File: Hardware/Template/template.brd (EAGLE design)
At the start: 39.4 x 39.4 mm, 24 parts, among them J1 10144517-042802LF, J2 10144518-041802LF, J3 10144517-042802LF, J4 10144518-041802LF, J6 2X5_0.05_SWD, U6 NCV8170AXV330T2G, U7 ATA6561-GAQW-N

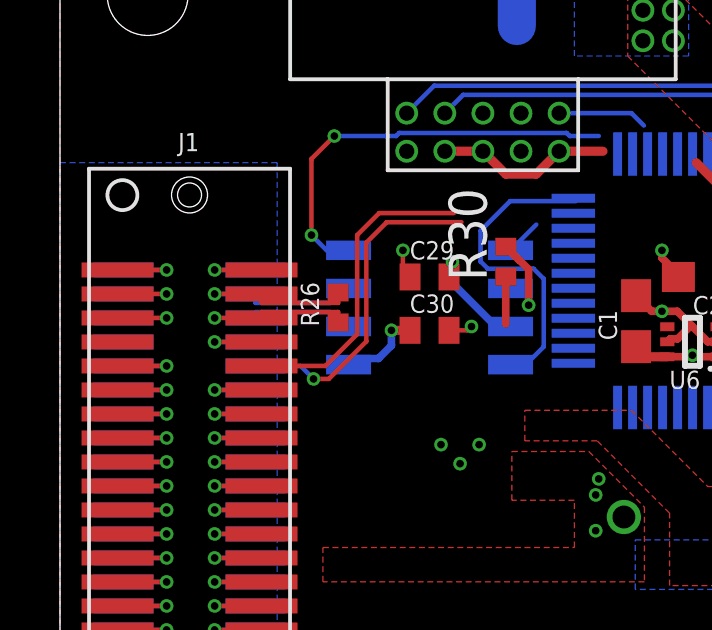
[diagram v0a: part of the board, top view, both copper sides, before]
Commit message: fixed power rail naming in template and added inventor drawing
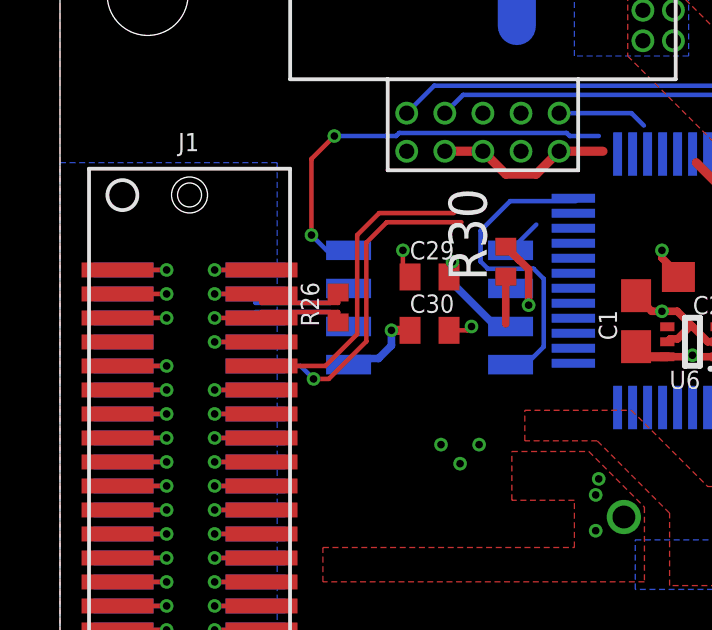
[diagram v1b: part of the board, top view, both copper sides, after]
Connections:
- new net +12V: J3.17, J3.19, J3.21, J3.23, J3.25, J3.27, J3.29, J4.17, J4.19, J4.21, J4.23, J4.25, J4.27, J4.29
- net +5V: no longer J3.17, J3.19, J3.21, J3.23, J3.25, J3.27, J3.29, J4.17, J4.19, J4.21, J4.23, J4.25, J4.27, J4.29
- net CAN0_N: now also J1.6
- net CAN_N: no longer J1.6
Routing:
- net +5V: track 10.9 -> 6.71 mm
- net +12V: track 0.00 -> 4.22 mm
- net CAN_N: track 7.96 -> 6.20 mm, vias 1 -> 0
- net CAN0_N: track 0.00 -> 1.56 mm, vias 0 -> 1
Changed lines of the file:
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@@
 <?xml version="1.0" encoding="utf-8"?>
 <!DOCTYPE eagle SYSTEM "eagle.dtd">
-<eagle version="9.5.2">
+<eagle version="9.6.0">
 <drawing>
 <settings>
-<setting alwaysvectorfont="no"/>
+<setting alwaysvectorfont="yes"/>
 <setting verticaltext="up"/>
 </settings>
@@
 </layers>
 <board>
-<fusionsync huburn="a.cGVyc29uYWw6dWUyZDEyOGNj" projecturn="a.cGVyc29uYWw6dWUyZDEyOGNjIzIwMTkwOTMwMjIwNjQ4MDc2" f3durn="urn:adsk.wipprod:dm.lineage:ArUQAsjyQquSRS0aqH2C6A" pcbguid="3c4015e3-43ac-4e19-9fe8-228eb0397e7d" lastpulledtime="" lastsyncedchangeguid="2c83db97-9ebd-c503-bffe-3982d56f7fbb"/>
+<fusionsync huburn="a.cGVyc29uYWw6dWUyZDEyOGNj" projecturn="a.cGVyc29uYWw6dWUyZDEyOGNjIzIwMTkwOTMwMjIwNjQ4MDc2" f3durn="urn:adsk.wipprod:dm.lineage:ArUQAsjyQquSRS0aqH2C6A" pcbguid="3c4015e3-43ac-4e19-9fe8-228eb0397e7d" lastpulledtime="" lastsyncedchangeguid="2c83db97-9ebd-c503-bffe-3982d56f7fbb" latestrevisionid="" lastsyncedrevisionid="" lastboardhashguid="" lastpushedtime="" linktopcb3d="%12"/>
 <plain>
 <wire x1="0" y1="36.449" x2="0" y2="2.921" width="0" layer="20"/>
@@
 <signal name="CAN_N">
 <contactref element="U7" pad="6"/>
-<contactref element="J1" pad="6"/>
-<wire x1="6.718" y1="25.685" x2="6.718" y2="25.8826" width="0.1524" layer="1"/>
 <wire x1="6.718" y1="25.8826" x2="9.271" y2="25.8826" width="0.1524" layer="1"/>
 <wire x1="9.271" y1="25.8826" x2="9.271" y2="25.535" width="0.1524" layer="1"/>
@@
 <wire x1="9.4996" y1="25.4" x2="9.017" y2="25.8826" width="0.1524" layer="16"/>
 <contactref element="R26" pad="1"/>
-<via x="5.154" y="25.685" extent="1-16" drill="0.254"/>
-<wire x1="5.154" y1="25.685" x2="6.718" y2="25.685" width="0.1524" layer="1"/>
-<wire x1="6.718" y1="25.685" x2="6.518" y2="25.8826" width="0" layer="19" extent="1-16"/>
+<wire x1="6.518" y1="25.8826" x2="6.718" y2="25.8826" width="0" layer="19" extent="1-16"/>
 </signal>
 <signal name="DETECT_A">
@@
 <wire x1="13.081" y1="26.8445" x2="13.081" y2="27.559" width="0.254" layer="16"/>
 <wire x1="14.5255" y1="25.4" x2="13.081" y2="26.8445" width="0.254" layer="16"/>
-<contactref element="J3" pad="29"/>
-<contactref element="J3" pad="17"/>
-<contactref element="J3" pad="19"/>
-<contactref element="J3" pad="21"/>
-<contactref element="J3" pad="23"/>
-<contactref element="J3" pad="25"/>
-<contactref element="J3" pad="27"/>
-<contactref element="J4" pad="17"/>
-<contactref element="J4" pad="19"/>
-<contactref element="J4" pad="21"/>
-<contactref element="J4" pad="23"/>
-<contactref element="J4" pad="25"/>
-<contactref element="J4" pad="27"/>
-<contactref element="J4" pad="29"/>
-<wire x1="33.106" y1="16.085" x2="33.4274" y2="16.4064" width="0.1524" layer="16"/>
 <via x="30.861" y="20.701" extent="1-16" drill="0.254"/>
 <polygon width="0.1524" layer="16" thermals="no">
@@
 <via x="31.115" y="20.193" extent="1-16" drill="0.254"/>
 <via x="31.369" y="19.685" extent="1-16" drill="0.254"/>
-<wire x1="30.601" y1="16.885" x2="33.106" y2="16.885" width="0.1524" layer="16"/>
-<wire x1="29.71" y1="15.994" x2="30.601" y2="16.885" width="0.1524" layer="16"/>
-<wire x1="32.906" y1="20.885" x2="33.106" y2="20.885" width="0" layer="19" extent="1-16"/>
-<wire x1="33.106" y1="20.085" x2="33.106" y2="20.885" width="0" layer="19" extent="16-16"/>
-<wire x1="32.906" y1="20.085" x2="33.106" y2="20.085" width="0" layer="19" extent="1-16"/>
-<wire x1="33.106" y1="19.285" x2="33.106" y2="20.085" width="0" layer="19" extent="16-16"/>
-<wire x1="32.906" y1="19.285" x2="33.106" y2="19.285" width="0" layer="19" extent="1-16"/>
-<wire x1="33.106" y1="18.485" x2="33.106" y2="19.285" width="0" layer="19" extent="16-16"/>
-<wire x1="32.906" y1="18.485" x2="33.106" y2="18.485" width="0" layer="19" extent="1-16"/>
-<wire x1="33.106" y1="17.685" x2="33.106" y2="18.485" width="0" layer="19" extent="16-16"/>
-<wire x1="32.906" y1="17.685" x2="33.106" y2="17.685" width="0" layer="19" extent="1-16"/>
-<wire x1="32.906" y1="16.885" x2="32.906" y2="17.685" width="0" layer="19" extent="1-1"/>
-<wire x1="33.106" y1="16.885" x2="32.906" y2="16.885" width="0" layer="19" extent="1-16"/>
-<wire x1="33.4274" y1="16.4064" x2="33.106" y2="16.885" width="0" layer="19" extent="16-16"/>
-<wire x1="32.906" y1="16.085" x2="33.106" y2="16.085" width="0" layer="19" extent="1-16"/>
-<wire x1="33.106" y1="15.285" x2="33.106" y2="16.085" width="0" layer="19" extent="16-16"/>
-<wire x1="32.906" y1="15.285" x2="33.106" y2="15.285" width="0" layer="19" extent="1-16"/>
+<wire x1="31.369" y1="20.701" x2="30.861" y2="20.701" width="0" layer="19" extent="1-1"/>
+<wire x1="31.115" y1="20.193" x2="30.861" y2="20.701" width="0" layer="19" extent="1-1"/>
+<wire x1="31.369" y1="19.685" x2="31.115" y2="20.193" width="0" layer="19" extent="1-1"/>
+<wire x1="32.906" y1="15.285" x2="31.369" y2="19.685" width="0" layer="19" extent="1-1"/>
+<wire x1="33.106" y1="15.285" x2="32.906" y2="15.285" width="0" layer="19" extent="1-16"/>
 <wire x1="33.106" y1="14.485" x2="33.106" y2="15.285" width="0" layer="19" extent="16-16"/>
 <wire x1="32.906" y1="14.485" x2="33.106" y2="14.485" width="0" layer="19" extent="1-16"/>
@@
 <wire x1="33.106" y1="12.885" x2="33.106" y2="13.685" width="0" layer="19" extent="16-16"/>
 <wire x1="32.906" y1="12.885" x2="33.106" y2="12.885" width="0" layer="19" extent="1-16"/>
-<wire x1="31.369" y1="20.701" x2="32.906" y2="20.885" width="0" layer="19" extent="1-1"/>
-<wire x1="30.861" y1="20.701" x2="31.369" y2="20.701" width="0" layer="19" extent="1-1"/>
-<wire x1="31.115" y1="20.193" x2="31.369" y2="20.701" width="0" layer="19" extent="1-1"/>
-<wire x1="31.369" y1="19.685" x2="31.115" y2="20.193" width="0" layer="19" extent="1-1"/>
 <wire x1="31.242" y1="14.732" x2="32.906" y2="14.485" width="0" layer="19" extent="1-1"/>
 <wire x1="31.242" y1="13.97" x2="31.242" y2="14.732" width="0" layer="19" extent="1-1"/>
@@
 <signal name="CAN0_N">
 <contactref element="J2" pad="6"/>
+<contactref element="J1" pad="6"/>
+<via x="5.154" y="25.685" extent="1-16" drill="0.254"/>
+<wire x1="5.154" y1="25.685" x2="6.718" y2="25.685" width="0.1524" layer="1"/>
+<wire x1="6.718" y1="25.685" x2="6.518" y2="25.685" width="0" layer="19" extent="1-16"/>
+</signal>
+<signal name="+12V">
+<contactref element="J3" pad="29"/>
+<contactref element="J3" pad="17"/>
+<contactref element="J3" pad="19"/>
+<contactref element="J3" pad="21"/>
+<contactref element="J3" pad="23"/>
+<contactref element="J3" pad="25"/>
+<contactref element="J3" pad="27"/>
+<contactref element="J4" pad="17"/>
+<contactref element="J4" pad="19"/>
+<contactref element="J4" pad="21"/>
+<contactref element="J4" pad="23"/>
+<contactref element="J4" pad="25"/>
+<contactref element="J4" pad="27"/>
+<contactref element="J4" pad="29"/>
+<wire x1="33.106" y1="16.085" x2="33.4274" y2="16.4064" width="0.1524" layer="16"/>
+<wire x1="30.601" y1="16.885" x2="33.106" y2="16.885" width="0.1524" layer="16"/>
+<wire x1="29.71" y1="15.994" x2="30.601" y2="16.885" width="0.1524" layer="16"/>
+<wire x1="32.906" y1="20.885" x2="33.106" y2="20.885" width="0" layer="19" extent="1-16"/>
+<wire x1="33.106" y1="20.085" x2="33.106" y2="20.885" width="0" layer="19" extent="16-16"/>
+<wire x1="32.906" y1="20.085" x2="33.106" y2="20.085" width="0" layer="19" extent="1-16"/>
+<wire x1="33.106" y1="19.285" x2="33.106" y2="20.085" width="0" layer="19" extent="16-16"/>
+<wire x1="32.906" y1="19.285" x2="33.106" y2="19.285" width="0" layer="19" extent="1-16"/>
+<wire x1="33.106" y1="18.485" x2="33.106" y2="19.285" width="0" layer="19" extent="16-16"/>
+<wire x1="32.906" y1="18.485" x2="33.106" y2="18.485" width="0" layer="19" extent="1-16"/>
+<wire x1="33.106" y1="17.685" x2="33.106" y2="18.485" width="0" layer="19" extent="16-16"/>
+<wire x1="32.906" y1="17.685" x2="33.106" y2="17.685" width="0" layer="19" extent="1-16"/>
+<wire x1="32.906" y1="16.885" x2="32.906" y2="17.685" width="0" layer="19" extent="1-1"/>
+<wire x1="33.106" y1="16.885" x2="32.906" y2="16.885" width="0" layer="19" extent="1-16"/>
+<wire x1="33.4274" y1="16.4064" x2="33.106" y2="16.885" width="0" layer="19" extent="16-16"/>
+<wire x1="32.906" y1="16.085" x2="33.106" y2="16.085" width="0" layer="19" extent="1-16"/>
 </signal>
 </signals>

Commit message: sims and some other stuff...
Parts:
- removed F1: (no value), adafruit:R1206
- removed U$13, U$9: WIRE-PAD, Wire Pads:12AWG-STRANDED
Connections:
- removed net +V_BAT_INT: F1.2
- removed net N$16: F1.1, U$13.P$1
- net PGND: no longer U$9.P$1
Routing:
- net N$16: track 6.96 -> 0.00 mm
- net +V_BAT_INT: track 4.19 -> 0.00 mm, vias 1 -> 0
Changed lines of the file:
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@@
 <attribute name="VALUE" x="9.398" y="28.575" size="1.27" layer="28" rot="MR270"/>
-</element>
-<element name="U$9" library="Wire Pads" package="12AWG-STRANDED" value="WIRE-PAD" x="30.48" y="36.957" smashed="yes" rot="R90"/>
-<element name="U$13" library="Wire Pads" package="12AWG-STRANDED" value="WIRE-PAD" x="24.511" y="36.83" smashed="yes" rot="R90"/>
-<element name="F1" library="adafruit" library_urn="urn:adsk.eagle:library:420" package="R1206" package3d_urn="urn:adsk.eagle:package:6240569/1" value="" x="16.383" y="37.4396" smashed="yes" rot="MR0">
-<attribute name="NAME" x="19.812" y="37.338" size="0.6096" layer="26" font="vector" rot="MR0"/>
-<attribute name="VALUE" x="17.78" y="35.0266" size="1.27" layer="28" rot="MR0"/>
 </element>
 <element name="R8" library="rcl" library_urn="urn:adsk.eagle:library:334" package="R0402" package3d_urn="urn:adsk.eagle:package:23547/3" value="" x="4.445" y="8.001" smashed="yes" rot="MR0">
@@
 </signal>
 <signal name="+V_BAT_INT">
-<contactref element="F1" pad="2"/>
-<wire x1="15.330375" y1="35.418825" x2="15.22753125" y2="35.415515625" width="0.1524" layer="16"/>
-<via x="13.589" y="37.973" extent="1-16" drill="0.254"/>
-<wire x1="14.961" y1="37.4396" x2="15.22753125" y2="37.17306875" width="1.27" layer="16"/>
-<wire x1="15.22753125" y1="37.17306875" x2="15.22753125" y2="35.415515625" width="1.27" layer="16"/>
-<wire x1="13.589" y1="37.973" x2="14.961" y2="37.973" width="0.1524" layer="16"/>
-<wire x1="14.961" y1="37.973" x2="14.961" y2="37.4396" width="0.1524" layer="16"/>
 <polygon width="0.508" layer="15">
 <vertex x="15.494" y="39.37"/>
@@
 <vertex x="15.494" y="37.338"/>
 </polygon>
-<wire x1="15.260846875" y1="35.3822" x2="15.22753125" y2="35.415515625" width="0.1524" layer="16"/>
 </signal>
 <signal name="P_GOOD">
@@
 <wire x1="33.401" y1="11.59" x2="33.401" y2="11.4554" width="0.1524" layer="1"/>
 </signal>
-<signal name="N$16">
-<contactref element="U$13" pad="P$1"/>
-<contactref element="F1" pad="1"/>
-<wire x1="17.805" y1="37.4396" x2="23.9014" y2="37.4396" width="1.27" layer="16"/>
-<wire x1="23.9014" y1="37.4396" x2="24.511" y2="36.83" width="1.27" layer="16"/>
-</signal>
 <signal name="RFU_37">
 <contactref element="J1" pad="37"/>
@@
 <contactref element="U6" pad="5"/>
 <contactref element="C1" pad="2"/>
-<contactref element="U$9" pad="P$1"/>
 <contactref element="J3" pad="2"/>
 <contactref element="J4" pad="40"/>
@@
 <vertex x="13.716" y="0"/>
 </polygon>
-<wire x1="36.068" y1="27.285" x2="30.48" y2="36.957" width="0" layer="19" extent="1-1"/>
 <wire x1="37.506" y1="26.485" x2="37.506" y2="27.285" width="0" layer="19" extent="16-16"/>
 <wire x1="37.506" y1="25.685" x2="37.506" y2="26.485" width="0" layer="19" extent="16-16"/>
